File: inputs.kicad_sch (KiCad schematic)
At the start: 16 parts

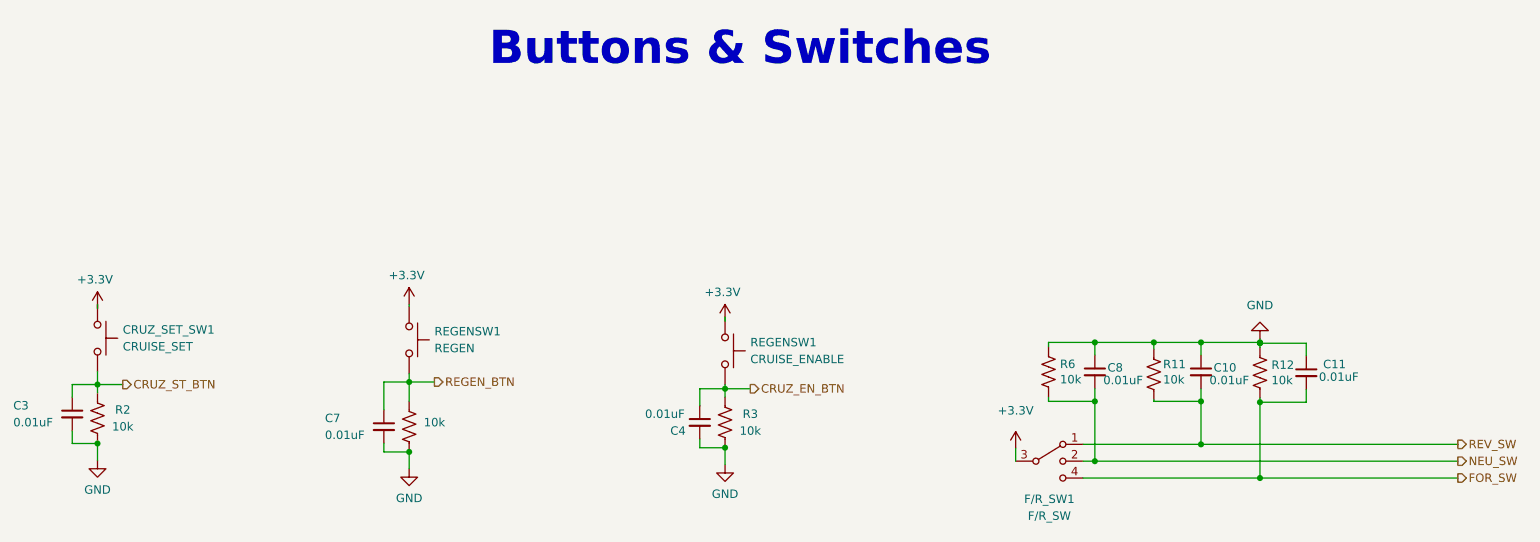
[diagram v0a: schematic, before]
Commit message: changed resistor values, updated footprints
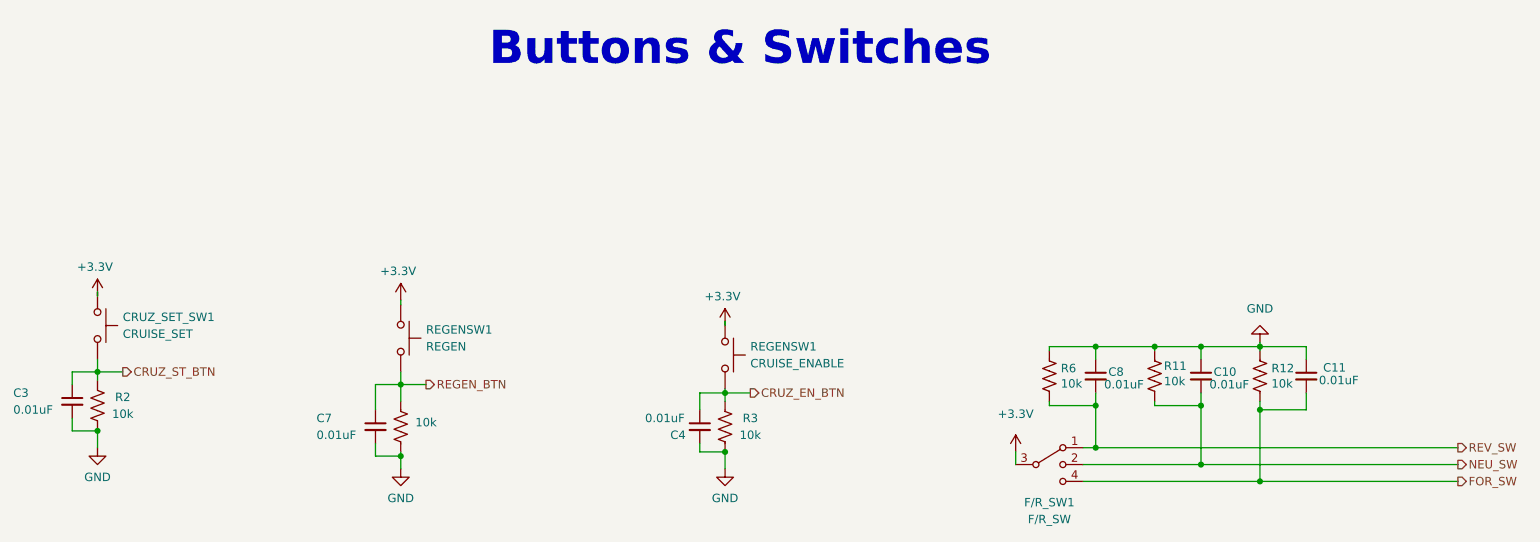
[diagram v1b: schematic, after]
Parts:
- C10, C11, C3, C4, C7, C8: Mouser Part Number (none) -> 80-C0805C103J5R
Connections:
- net NEU_SW: now also C10.2, R11.2; no longer C8.2, R6.2
- net REV_SW: now also C8.2, R6.2; no longer C10.2, R11.2
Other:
- moved on the sheet: C10, C11, C3, C4, C7, C8, CRUZ_SET_SW1, F/R_SW1, R12, R2, R3, R6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

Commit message: Added resistor to fan isolator, fixed ERC errors and warnings
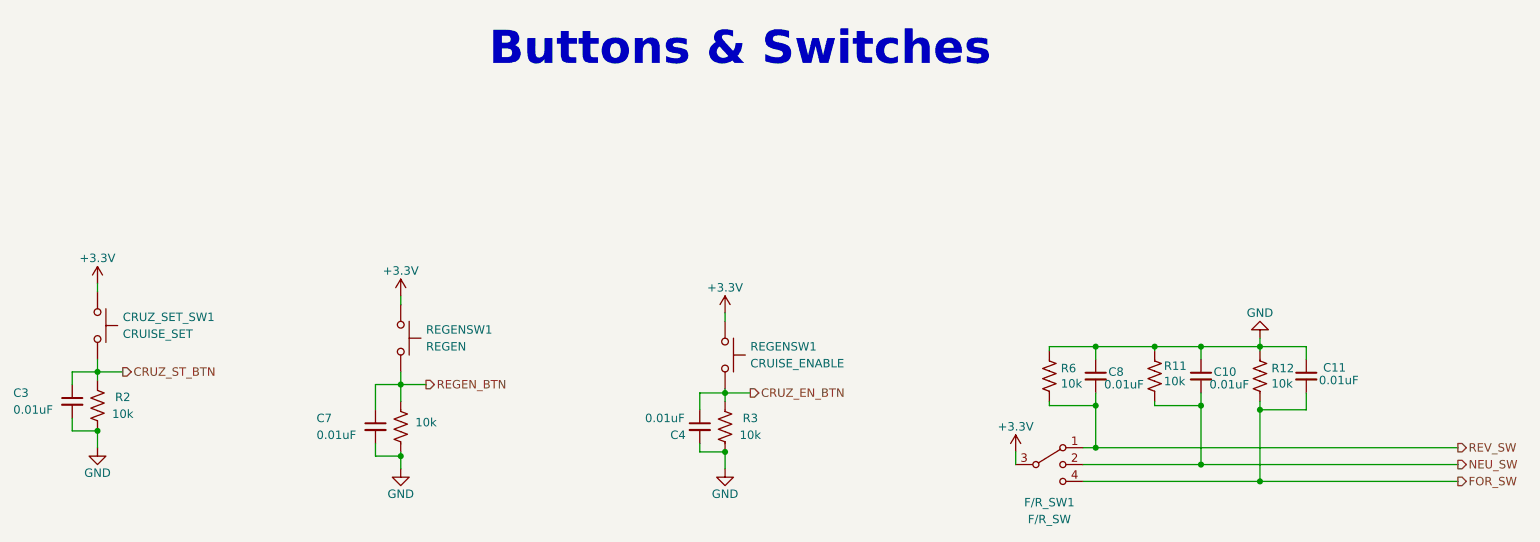
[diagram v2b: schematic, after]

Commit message: changed labels for some connectors
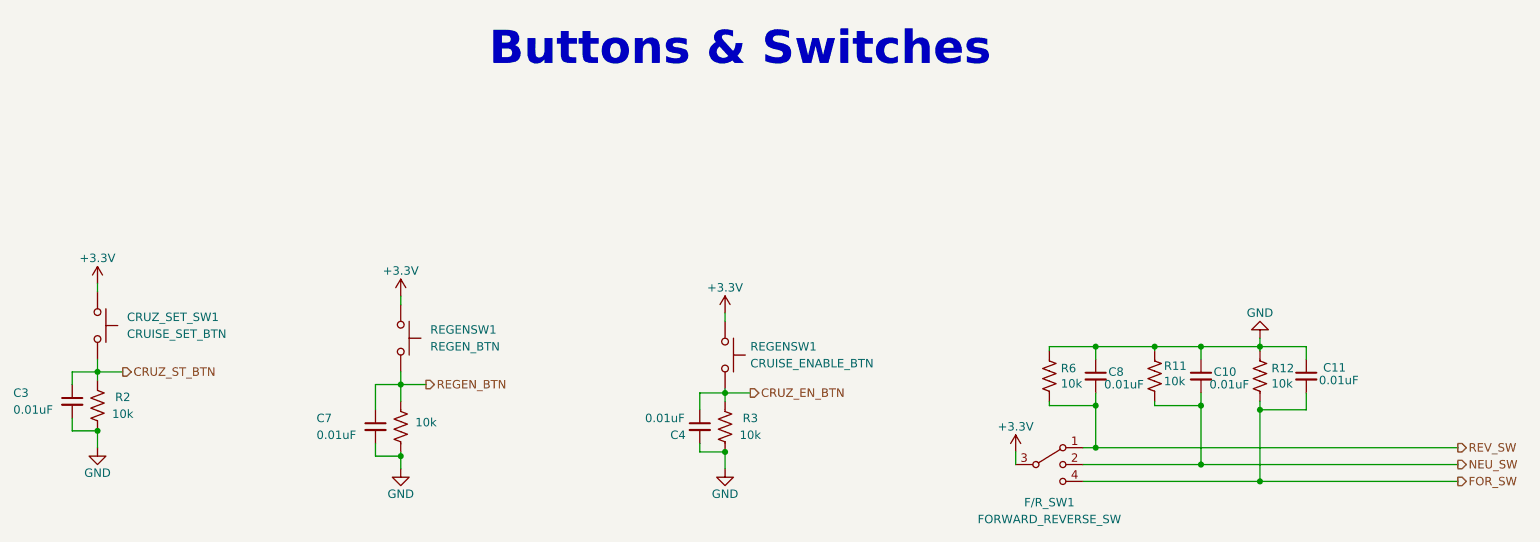
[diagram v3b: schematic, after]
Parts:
- CRUZ_SET_SW1: value CRUISE_SET -> CRUISE_SET_BTN
- F/R_SW1: value F/R_SW -> FORWARD_REVERSE_SW
- REGENSW1: value REGEN -> REGEN_BTN
- REGENSW1: value CRUISE_ENABLE -> CRUISE_ENABLE_BTN
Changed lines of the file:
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@@
   (symbol (lib_id "Switch:SW_Push") (at 93.345 103.505 270) (unit 1)
     (in_bom yes) (on_board yes) (dnp no) (fields_autoplaced)
-    (property "Reference" "REGENSW1" (at 97.155 102.235 90)
-      (effects (font (size 1.27 1.27)) (justify left))
-    )
-    (property "Value" "REGEN" (at 97.155 104.775 90)
+    (property "Reference" "REGENSW1" (at 97.79 102.235 90)
+      (effects (font (size 1.27 1.27)) (justify left))
+    )
+    (property "Value" "REGEN_BTN" (at 97.79 104.775 90)
       (effects (font (size 1.27 1.27)) (justify left))
     )
@@
       (project "Controls-DaughterPCB"
         (path "/c7871779-04fe-4705-8150-20a4dd0ef44f/baa2171f-2fe6-4866-b55f-9d97b4b1290e"
-          (reference "REGEN_BTN1") (unit 1)
+          (reference "REGEN1") (unit 1)
         )
       )
@@
       (effects (font (size 1.27 1.27)) (justify left))
     )
-    (property "Value" "CRUISE_ENABLE" (at 146.05 107.315 90)
+    (property "Value" "CRUISE_ENABLE_BTN" (at 146.05 107.315 90)
       (effects (font (size 1.27 1.27)) (justify left))
     )
@@
       (project "Controls-DaughterPCB"
         (path "/c7871779-04fe-4705-8150-20a4dd0ef44f/baa2171f-2fe6-4866-b55f-9d97b4b1290e"
-          (reference "CRUZ_EN_BTN1") (unit 1)
+          (reference "CRUZ_EN1") (unit 1)
         )
       )
@@
   (symbol (lib_id "Switch:SW_Push") (at 47.625 101.6 270) (unit 1)
     (in_bom yes) (on_board yes) (dnp no) (fields_autoplaced)
-    (property "Reference" "CRUZ_SET_SW1" (at 51.435 100.33 90)
-      (effects (font (size 1.27 1.27)) (justify left))
-    )
-    (property "Value" "CRUISE_SET" (at 51.435 102.87 90)
+    (property "Reference" "CRUZ_SET_SW1" (at 52.07 100.33 90)
+      (effects (font (size 1.27 1.27)) (justify left))
+    )
+    (property "Value" "CRUISE_SET_BTN" (at 52.07 102.87 90)
       (effects (font (size 1.27 1.27)) (justify left))
     )
@@
       (project "Controls-DaughterPCB"
         (path "/c7871779-04fe-4705-8150-20a4dd0ef44f/baa2171f-2fe6-4866-b55f-9d97b4b1290e"
-          (reference "CRUZ_SET_BTN1") (unit 1)
+          (reference "CRUZ_SET1") (unit 1)
         )
       )
@@
       (effects (font (size 1.27 1.27)))
     )
-    (property "Value" "F/R_SW" (at 191.135 130.81 0)
+    (property "Value" "FORWARD_REVERSE_SW" (at 191.135 130.81 0)
       (effects (font (size 1.27 1.27)))
     )
@@
       (project "Controls-DaughterPCB"
         (path "/c7871779-04fe-4705-8150-20a4dd0ef44f/baa2171f-2fe6-4866-b55f-9d97b4b1290e"
-          (reference "F/R_SW1") (unit 1)
-        )
-      )
+          (reference "FR1") (unit 1)
+        )
+      )

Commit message: updated footprints and part numbers, added motor CAN 12V connection
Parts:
- C10, C11, C3, C4, C7, C8: Mauser PN (none) -> 80-C0805C103J5R; Mouser Part Number 80-C0805C103J5R -> (none); P/N C0805C103J5RACTU -> (none); PN (none) -> C0805C103J5RACTU
- CRUZ_SET_SW1, REGENSW1: Mauser PN (none) -> 538-43650-0215; P/N 43650-0215 -> (none); PN (none) -> 43650-0215
- F/R_SW1: Mauser PN (none) -> 538-43650-0415; P/N 43650-0415 -> (none); PN (none) -> 43650-0415
- R11, R12, R2, R3, R6, R7: Mauser PN (none) -> 71-CRCW080510K0FKEAC; P/N CRCW080510K0FKEAC -> (none); PN (none) -> CRCW080510K0FKEAC
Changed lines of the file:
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@@
       (effects (font (size 1.27 1.27)) hide)
     )
-    (property "Datasheet" "~" (at 43.815 113.03 0)
-      (effects (font (size 1.27 1.27)) hide)
-    )
-    (property "P/N" "C0805C103J5RACTU" (at 43.815 113.03 0)
-      (effects (font (size 1.27 1.27)) hide)
-    )
-    (property "Mouser Part Number" "80-C0805C103J5R" (at 43.815 113.03 0)
+    (property "Datasheet" "https://www.mouser.com/datasheet/2/447/KEM_C1002_X7R_SMD-3316098.pdf" (at 43.815 113.03 0)
+      (effects (font (size 1.27 1.27)) hide)
+    )
+    (property "PN" "C0805C103J5RACTU" (at 43.815 113.03 0)
+      (effects (font (size 1.27 1.27)) hide)
+    )
+    (property "Mauser PN" "80-C0805C103J5R" (at 43.815 113.03 0)
       (effects (font (size 1.27 1.27)) hide)
     )
@@
       (effects (font (size 1.27 1.27)) hide)
     )
-    (property "Datasheet" "~" (at 198.12 109.22 0)
-      (effects (font (size 1.27 1.27)) hide)
-    )
-    (property "P/N" "C0805C103J5RACTU" (at 198.12 109.22 0)
-      (effects (font (size 1.27 1.27)) hide)
-    )
-    (property "Mouser Part Number" "80-C0805C103J5R" (at 198.12 109.22 0)
+    (property "Datasheet" "https://www.mouser.com/datasheet/2/447/KEM_C1002_X7R_SMD-3316098.pdf" (at 198.12 109.22 0)
+      (effects (font (size 1.27 1.27)) hide)
+    )
+    (property "PN" "C0805C103J5RACTU" (at 198.12 109.22 0)
+      (effects (font (size 1.27 1.27)) hide)
+    )
+    (property "Mauser PN" "80-C0805C103J5R" (at 198.12 109.22 0)
       (effects (font (size 1.27 1.27)) hide)
     )
@@
       (effects (font (size 1.27 1.27)) hide)
     )
-    (property "Datasheet" "~" (at 207.01 109.22 0)
-      (effects (font (size 1.27 1.27)) hide)
-    )
-    (property "P/N" "CRCW080510K0FKEAC" (at 207.01 109.22 0)
+    (property "Datasheet" "https://www.vishay.com/docs/28773/crcwce3.pdf" (at 207.01 109.22 0)
+      (effects (font (size 1.27 1.27)) hide)
+    )
+    (property "PN" "CRCW080510K0FKEAC" (at 207.01 109.22 0)
+      (effects (font (size 1.27 1.27)) hide)
+    )
+    (property "Mauser PN" "71-CRCW080510K0FKEAC " (at 207.01 109.22 0)
       (effects (font (size 1.27 1.27)) hide)
     )
@@
       (effects (font (size 1.27 1.27)) hide)
     )
-    (property "P/N" "43650-0215" (at 93.345 103.505 90)
+    (property "PN" "43650-0215" (at 93.345 103.505 0)
+      (effects (font (size 1.27 1.27)) hide)
+    )
+    (property "Mauser PN" "538-43650-0215" (at 93.345 103.505 0)
       (effects (font (size 1.27 1.27)) hide)
     )
@@
       (effects (font (size 1.27 1.27)) hide)
     )
-    (property "Datasheet" "~" (at 213.995 109.22 0)
-      (effects (font (size 1.27 1.27)) hide)
-    )
-    (property "P/N" "C0805C103J5RACTU" (at 213.995 109.22 0)
-      (effects (font (size 1.27 1.27)) hide)
-    )
-    (property "Mouser Part Number" "80-C0805C103J5R" (at 213.995 109.22 0)
+    (property "Datasheet" "https://www.mouser.com/datasheet/2/447/KEM_C1002_X7R_SMD-3316098.pdf" (at 213.995 109.22 0)
+      (effects (font (size 1.27 1.27)) hide)
+    )
+    (property "PN" "C0805C103J5RACTU" (at 213.995 109.22 0)
+      (effects (font (size 1.27 1.27)) hide)
+    )
+    (property "Mauser PN" "80-C0805C103J5R" (at 213.995 109.22 0)
       (effects (font (size 1.27 1.27)) hide)
     )
@@
       (effects (font (size 1.27 1.27)) hide)
     )
-    (property "P/N" "43650-0215" (at 142.24 106.045 90)
+    (property "PN" "43650-0215" (at 142.24 106.045 0)
+      (effects (font (size 1.27 1.27)) hide)
+    )
+    (property "Mauser PN" "538-43650-0215" (at 142.24 106.045 0)
       (effects (font (size 1.27 1.27)) hide)
     )
@@
       (effects (font (size 1.27 1.27)) hide)
     )
-    (property "Datasheet" "~" (at 89.535 116.84 0)
-      (effects (font (size 1.27 1.27)) hide)
-    )
-    (property "P/N" "C0805C103J5RACTU" (at 89.535 116.84 0)
-      (effects (font (size 1.27 1.27)) hide)
-    )
-    (property "Mouser Part Number" "80-C0805C103J5R" (at 89.535 116.84 0)
+    (property "Datasheet" "https://www.mouser.com/datasheet/2/447/KEM_C1002_X7R_SMD-3316098.pdf" (at 89.535 116.84 0)
+      (effects (font (size 1.27 1.27)) hide)
+    )
+    (property "PN" "C0805C103J5RACTU" (at 89.535 116.84 0)
+      (effects (font (size 1.27 1.27)) hide)
+    )
+    (property "Mauser PN" "80-C0805C103J5R" (at 89.535 116.84 0)
       (effects (font (size 1.27 1.27)) hide)
     )
@@
       (effects (font (size 1.27 1.27)) hide)
     )
-    (property "Datasheet" "~" (at 142.24 116.84 0)
-      (effects (font (size 1.27 1.27)) hide)
-    )
-    (property "P/N" "CRCW080510K0FKEAC" (at 142.24 116.84 0)
+    (property "Datasheet" "https://www.vishay.com/docs/28773/crcwce3.pdf" (at 142.24 116.84 0)
+      (effects (font (size 1.27 1.27)) hide)
+    )
+    (property "PN" "CRCW080510K0FKEAC" (at 142.24 116.84 0)
+      (effects (font (size 1.27 1.27)) hide)
+    )
+    (property "Mauser PN" "71-CRCW080510K0FKEAC " (at 142.24 116.84 0)
       (effects (font (size 1.27 1.27)) hide)
     )
@@
       (effects (font (size 1.27 1.27)) hide)
     )
-    (property "P/N" "43650-0215" (at 47.625 101.6 90)
+    (property "PN" "43650-0215" (at 47.625 101.6 0)
+      (effects (font (size 1.27 1.27)) hide)
+    )
+    (property "Mauser PN" "538-43650-0215" (at 47.625 101.6 0)
       (effects (font (size 1.27 1.27)) hide)
     )
@@
       (effects (font (size 1.27 1.27)) hide)
     )
-    (property "P/N" "43650-0415" (at 191.135 122.555 0)
+    (property "PN" "43650-0415" (at 191.135 122.555 0)
+      (effects (font (size 1.27 1.27)) hide)
+    )
+    (property "Mauser PN" "538-43650-0415" (at 191.135 122.555 0)
       (effects (font (size 1.27 1.27)) hide)
     )
@@
       (effects (font (size 1.27 1.27)) hide)
     )
-    (property "Datasheet" "~" (at 222.885 109.22 0)
-      (effects (font (size 1.27 1.27)) hide)
-    )
-    (property "P/N" "CRCW080510K0FKEAC" (at 222.885 109.22 0)
+    (property "Datasheet" "https://www.vishay.com/docs/28773/crcwce3.pdf" (at 222.885 109.22 0)
+      (effects (font (size 1.27 1.27)) hide)
+    )
+    (property "PN" "CRCW080510K0FKEAC" (at 222.885 109.22 0)
+      (effects (font (size 1.27 1.27)) hide)
+    )
+    (property "Mauser PN" "71-CRCW080510K0FKEAC " (at 222.885 109.22 0)
       (effects (font (size 1.27 1.27)) hide)
     )
@@
       (effects (font (size 1.27 1.27)) hide)
     )
-    (property "Datasheet" "~" (at 229.87 109.22 0)
-      (effects (font (size 1.27 1.27)) hide)
-    )
-    (property "P/N" "C0805C103J5RACTU" (at 229.87 109.22 0)
-      (effects (font (size 1.27 1.27)) hide)
-    )
-    (property "Mouser Part Number" "80-C0805C103J5R" (at 229.87 109.22 0)
+    (property "Datasheet" "https://www.mouser.com/datasheet/2/447/KEM_C1002_X7R_SMD-3316098.pdf" (at 229.87 109.22 0)
+      (effects (font (size 1.27 1.27)) hide)
+    )
+    (property "PN" "C0805C103J5RACTU" (at 229.87 109.22 0)
+      (effects (font (size 1.27 1.27)) hide)
+    )
+    (property "Mauser PN" "80-C0805C103J5R" (at 229.87 109.22 0)
       (effects (font (size 1.27 1.27)) hide)
     )
@@
       (effects (font (size 1.27 1.27)) hide)
     )
-    (property "Datasheet" "~" (at 47.625 113.665 0)
-      (effects (font (size 1.27 1.27)) hide)
-    )
-    (property "P/N" "CRCW080510K0FKEAC" (at 47.625 113.665 0)
+    (property "Datasheet" "https://www.vishay.com/docs/28773/crcwce3.pdf" (at 47.625 113.665 0)
+      (effects (font (size 1.27 1.27)) hide)
+    )
+    (property "PN" "CRCW080510K0FKEAC" (at 47.625 113.665 0)
+      (effects (font (size 1.27 1.27)) hide)
+    )
+    (property "Mauser PN" "71-CRCW080510K0FKEAC " (at 47.625 113.665 0)
       (effects (font (size 1.27 1.27)) hide)
     )
@@
       (effects (font (size 1.27 1.27)) hide)
     )
-    (property "Datasheet" "~" (at 93.345 116.84 0)
-      (effects (font (size 1.27 1.27)) hide)
-    )
-    (property "P/N" "CRCW080510K0FKEAC" (at 93.345 116.84 0)
+    (property "Datasheet" "https://www.vishay.com/docs/28773/crcwce3.pdf" (at 93.345 116.84 0)
+      (effects (font (size 1.27 1.27)) hide)
+    )
+    (property "PN" "CRCW080510K0FKEAC" (at 93.345 116.84 0)
+      (effects (font (size 1.27 1.27)) hide)
+    )
+    (property "Mauser PN" "71-CRCW080510K0FKEAC " (at 93.345 116.84 0)
       (effects (font (size 1.27 1.27)) hide)
     )
@@
       (effects (font (size 1.27 1.27)) hide)
     )
-    (property "Datasheet" "~" (at 138.43 116.84 0)
-      (effects (font (size 1.27 1.27)) hide)
-    )
-    (property "P/N" "C0805C103J5RACTU" (at 138.43 116.84 0)
-      (effects (font (size 1.27 1.27)) hide)
-    )
-    (property "Mouser Part Number" "80-C0805C103J5R" (at 138.43 116.84 0)
+    (property "Datasheet" "https://www.mouser.com/datasheet/2/447/KEM_C1002_X7R_SMD-3316098.pdf" (at 138.43 116.84 0)
+      (effects (font (size 1.27 1.27)) hide)
+    )
+    (property "PN" "C0805C103J5RACTU" (at 138.43 116.84 0)
+      (effects (font (size 1.27 1.27)) hide)
+    )
+    (property "Mauser PN" "80-C0805C103J5R" (at 138.43 116.84 0)
       (effects (font (size 1.27 1.27)) hide)
     )
@@
       (effects (font (size 1.27 1.27)) hide)
     )
-    (property "Datasheet" "~" (at 191.135 109.22 0)
-      (effects (font (size 1.27 1.27)) hide)
-    )
-    (property "P/N" "CRCW080510K0FKEAC" (at 191.135 109.22 0)
-      (effects (font (size 1.27 1.27)) hide)
-    )
+    (property "Datasheet" "https://www.vishay.com/docs/28773/crcwce3.pdf" (at 191.135 109.22 0)
+      (effects (font (size 1.27 1.27)) hide)
+    )
+    (property "PN" "CRCW080510K0FKEAC" (at 191.135 109.22 0)
+      (effects (font (size 1.27 1.27)) hide)
+    )
+    (property "Mauser PN" "71-CRCW080510K0FKEAC " (at 191.135 109.22 0)
+      (effects (font (size 1.27 1.27)) hide)
+    )

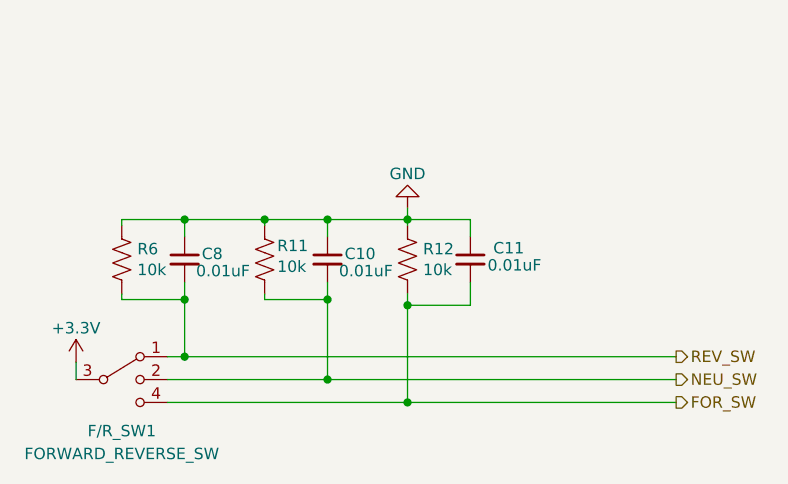
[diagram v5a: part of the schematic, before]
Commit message: Removed neutral section's debouncing circuitry and connections
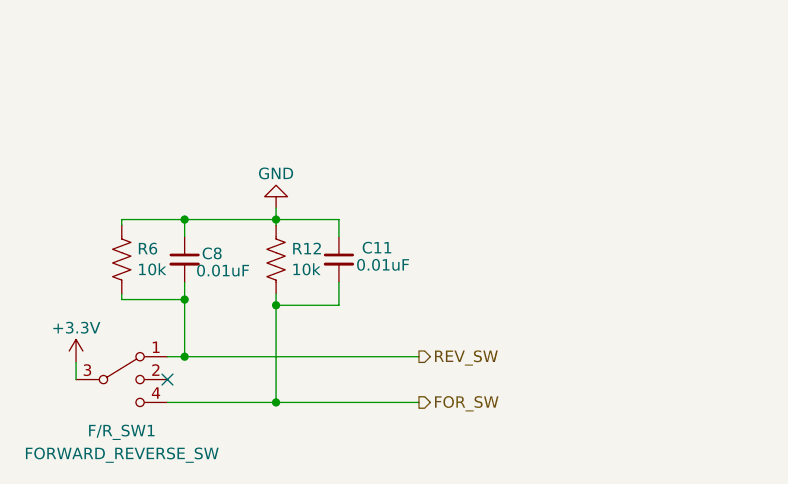
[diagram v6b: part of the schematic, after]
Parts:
- removed C10: 0.01uF, Capacitor_SMD:C_0805_2012Metric, symbol Device:C_Small
- removed R11: 10k, Resistor_SMD:R_0805_2012Metric, symbol Device:R_US
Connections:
- net NEU_SW: no longer names the net of F/R_SW1.2
- no-connect marks 0 -> 1
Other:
- moved on the sheet: C11, R12
